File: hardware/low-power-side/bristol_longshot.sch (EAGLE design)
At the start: 80 parts, among them U1 SAM_D20E, U10 ADP1607ACPZN-R7, U11 TPS73118DBVT, U12 TPS73118DBVT, U14 SIT1552, U15 LIS2DH, U16 SIT1552, U2 SI4060, U3 SE880, U4 SST25WF040BT-40I/NP, U5 TG-5006CJ, U6 TG-5006CJ, U7 TPS3123, U8 SN74LVC1G32DCKR, U9 MS5607-02BA03

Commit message: [low-power] v0.986.8. Changed memory pads, GPS LDO and specified SAMD20E18A-MN with more flash and higher grade packaging
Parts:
- removed U4: SST25WF040BT-40I/NP, fbri:SST25WF040BT-40I/NP
- added U$80: SST25WF040BT-40I/NP, fbri:SST25WF040BT-40I/NP
- C11: value 10nF -> DNP
- U12: value TPS73118DBVT -> MIC94310-GYM5
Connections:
- net 1.8V: now also C22.P$1, U$80.!HOLD, U$80.VDD; no longer C14.P$1, U4.!HOLD, U4.VDD
- net GND: now also U$80.VSS; no longer U4.GND_PAD, U4.VSS
- net MEM_CSN: now also U$80.!CE; no longer U4.!CE
- net MEM_MISO: now also U$80.SO/SIO1; no longer U4.SO/SIO1
- net MEM_MOSI: now also U$80.SI/SIO0; no longer U4.SI/SIO0
- net MEM_SCK: now also U$80.SCK; no longer U4.SCK
- net MEM_WPN: now also U$80.!WP; no longer U4.!WP
- net TCXO_VDD1: now also C14.P$1; no longer C22.P$1
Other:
- note added: "XFL4020 is better than VLF302512MT-2R2M used for datasheet efficiency measurements"
- moved on the sheet: C14, C22
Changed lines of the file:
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@@
 <part name="C17" library="microbuilder_v3" deviceset="CAP_CERAMIC" device="_0402" value="100nF"/>
 <part name="U$78" library="microbuilder_v3" deviceset="GND" device=""/>
-<part name="U4" library="fbri" deviceset="SST25WF040BT-40I/NP" device=""/>
 <part name="U$22" library="microbuilder_v3" deviceset="GND" device=""/>
 <part name="JTAG1" library="microbuilder_v3" deviceset="JTAG-CORTEXM3" device="SMT"/>
@@
 <part name="L9" library="Coilcraft_XAL" deviceset="EPL2010" device="" value="EPL2010-2.2µH"/>
 <part name="C27" library="microbuilder_v3" deviceset="CAP_CERAMIC" device="_0402" value="1nF"/>
-<part name="C22" library="microbuilder_v3" deviceset="CAP_CERAMIC" device="_0402" value="100nF"/>
+<part name="C14" library="microbuilder_v3" deviceset="CAP_CERAMIC" device="_0402" value="100nF"/>
 <part name="C31" library="resistor" deviceset="C-EU" device="C0603K" value="10µF"/>
 <part name="U11" library="TPS73118DVBT" deviceset="TPS73118DBVT" device=""/>
@@
 <part name="U14" library="fbri" deviceset="SIT1552" device=""/>
 <part name="U$71" library="microbuilder_v3" deviceset="GND" device=""/>
-<part name="U12" library="TPS73118DVBT" deviceset="TPS73118DBVT" device=""/>
+<part name="U12" library="TPS73118DVBT" deviceset="TPS73118DBVT" device="" value="MIC94310-GYM5"/>
 <part name="U$70" library="microbuilder_v3" deviceset="1.8V" device=""/>
-<part name="C11" library="microbuilder_v3" deviceset="CAP_CERAMIC" device="_0402" value="10nF"/>
+<part name="C11" library="microbuilder_v3" deviceset="CAP_CERAMIC" device="_0402" value="DNP"/>
 <part name="U$84" library="microbuilder_v3" deviceset="GND" device=""/>
 <part name="U$85" library="microbuilder_v3" deviceset="GND" device=""/>
-<part name="C14" library="microbuilder_v3" deviceset="CAP_CERAMIC" device="_0402" value="100nF"/>
+<part name="C22" library="microbuilder_v3" deviceset="CAP_CERAMIC" device="_0402" value="100nF"/>
 <part name="U$65" library="microbuilder_v3" deviceset="GND" device=""/>
 <part name="U16" library="fbri" deviceset="SIT1552" device=""/>
@@
 <part name="U$76" library="microbuilder_v3" deviceset="GND" device=""/>
 <part name="U$77" library="microbuilder_v3" deviceset="1.8V" device=""/>
+<part name="U$80" library="fbri" deviceset="SST25WF040BT-40I/NP" device=""/>
 </parts>
 <sheets>
@@
 <text x="256.54" y="122.428" size="1.27" layer="97" font="vector" ratio="11" distance="100">C15 in close
 proximity</text>
+<text x="27.94" y="66.548" size="1.27" layer="97" font="vector" ratio="11" distance="100">XFL4020 is better than
+VLF302512MT-2R2M used for
+datasheet efficiency
+measurements</text>
 </plain>
 <instances>
@@
 <instance part="C17" gate="G$1" x="20.32" y="172.72"/>
 <instance part="U$78" gate="G$1" x="20.32" y="165.1"/>
-<instance part="U4" gate="G$1" x="226.06" y="83.82"/>
 <instance part="U$22" gate="G$1" x="55.88" y="213.36" rot="MR0"/>
 <instance part="JTAG1" gate="G$1" x="43.18" y="226.06" rot="MR0"/>
@@
 <instance part="L9" gate="G$1" x="706.12" y="106.68"/>
 <instance part="C27" gate="G$1" x="726.44" y="91.44"/>
-<instance part="C22" gate="G$1" x="739.14" y="91.44"/>
+<instance part="C14" gate="G$1" x="739.14" y="91.44"/>
 <instance part="C31" gate="G$1" x="751.84" y="93.98"/>
 <instance part="U11" gate="A" x="492.76" y="208.28"/>
@@
 <instance part="U$84" gate="G$1" x="502.92" y="76.2"/>
 <instance part="U$85" gate="G$1" x="492.76" y="76.2"/>
-<instance part="C14" gate="G$1" x="459.74" y="88.9"/>
+<instance part="C22" gate="G$1" x="459.74" y="88.9"/>
 <instance part="U$65" gate="G$1" x="459.74" y="76.2"/>
 <instance part="U16" gate="G$1" x="241.3" y="121.92" rot="MR0"/>
@@
 <instance part="U$76" gate="G$1" x="134.62" y="213.36" rot="MR0"/>
 <instance part="U$77" gate="G$1" x="134.62" y="254" rot="MR0"/>
+<instance part="U$80" gate="G$1" x="228.6" y="83.82"/>
 </instances>
 <busses>
@@
 <segment>
 <pinref part="U$39" gate="G$1" pin="GND"/>
-<wire x1="205.74" y1="78.74" x2="195.58" y2="78.74" width="0.1524" layer="91"/>
+<wire x1="208.28" y1="78.74" x2="195.58" y2="78.74" width="0.1524" layer="91"/>
 <wire x1="195.58" y1="78.74" x2="185.42" y2="78.74" width="0.1524" layer="91"/>
-<wire x1="185.42" y1="78.74" x2="185.42" y2="76.2" width="0.1524" layer="91"/>
-<wire x1="185.42" y1="76.2" x2="185.42" y2="73.66" width="0.1524" layer="91"/>
-<wire x1="205.74" y1="76.2" x2="185.42" y2="76.2" width="0.1524" layer="91"/>
-<junction x="185.42" y="76.2"/>
+<wire x1="185.42" y1="78.74" x2="185.42" y2="73.66" width="0.1524" layer="91"/>
 <pinref part="C21" gate="G$1" pin="P$2"/>
 <wire x1="185.42" y1="78.74" x2="185.42" y2="81.28" width="0.1524" layer="91"/>
 <junction x="185.42" y="78.74"/>
-<pinref part="U4" gate="G$1" pin="VSS"/>
-<pinref part="U4" gate="G$1" pin="GND_PAD"/>
 <pinref part="C10" gate="G$1" pin="P$2"/>
 <wire x1="195.58" y1="81.28" x2="195.58" y2="78.74" width="0.1524" layer="91"/>
 <junction x="195.58" y="78.74"/>
+<pinref part="U$80" gate="G$1" pin="VSS"/>
 </segment>
 <segment>
@@
 <wire x1="726.44" y1="88.9" x2="739.14" y2="88.9" width="0.1524" layer="91"/>
 <junction x="726.44" y="88.9"/>
-<pinref part="C22" gate="G$1" pin="P$2"/>
+<pinref part="C14" gate="G$1" pin="P$2"/>
 <wire x1="739.14" y1="88.9" x2="751.84" y2="88.9" width="0.1524" layer="91"/>
 <junction x="739.14" y="88.9"/>
@@
 </segment>
 <segment>
-<pinref part="C14" gate="G$1" pin="P$2"/>
+<pinref part="C22" gate="G$1" pin="P$2"/>
 <pinref part="U$65" gate="G$1" pin="GND"/>
 <wire x1="459.74" y1="86.36" x2="459.74" y2="78.74" width="0.1524" layer="91"/>
@@
 <net name="MEM_MOSI" class="0">
 <segment>
-<wire x1="246.38" y1="91.44" x2="264.16" y2="91.44" width="0.1524" layer="91"/>
+<wire x1="248.92" y1="91.44" x2="264.16" y2="91.44" width="0.1524" layer="91"/>
 <label x="251.46" y="91.44" size="1.778" layer="95" ratio="11"/>
-<pinref part="U4" gate="G$1" pin="SI/SIO0"/>
+<pinref part="U$80" gate="G$1" pin="SI/SIO0"/>
 </segment>
 <segment>
@@
 <net name="MEM_CSN" class="0">
 <segment>
-<wire x1="264.16" y1="78.74" x2="246.38" y2="78.74" width="0.1524" layer="91"/>
+<wire x1="264.16" y1="78.74" x2="248.92" y2="78.74" width="0.1524" layer="91"/>
 <label x="251.46" y="78.74" size="1.778" layer="95" ratio="11"/>
-<pinref part="U4" gate="G$1" pin="!CE"/>
+<pinref part="U$80" gate="G$1" pin="!CE"/>
 </segment>
 <segment>
@@
 <net name="MEM_WPN" class="0">
 <segment>
-<wire x1="246.38" y1="81.28" x2="264.16" y2="81.28" width="0.1524" layer="91"/>
+<wire x1="248.92" y1="81.28" x2="264.16" y2="81.28" width="0.1524" layer="91"/>
 <label x="251.46" y="81.28" size="1.778" layer="95" ratio="11"/>
-<pinref part="U4" gate="G$1" pin="!WP"/>
+<pinref part="U$80" gate="G$1" pin="!WP"/>
 </segment>
 </net>
@@
 <net name="MEM_SCK" class="0">
 <segment>
-<wire x1="246.38" y1="86.36" x2="264.16" y2="86.36" width="0.1524" layer="91"/>
+<wire x1="248.92" y1="86.36" x2="264.16" y2="86.36" width="0.1524" layer="91"/>
 <label x="251.46" y="86.36" size="1.778" layer="95" ratio="11"/>
-<pinref part="U4" gate="G$1" pin="SCK"/>
+<pinref part="U$80" gate="G$1" pin="SCK"/>
 </segment>
 <segment>
@@
 <net name="MEM_MISO" class="0">
 <segment>
-<wire x1="246.38" y1="88.9" x2="264.16" y2="88.9" width="0.1524" layer="91"/>
+<wire x1="248.92" y1="88.9" x2="264.16" y2="88.9" width="0.1524" layer="91"/>
 <label x="251.46" y="88.9" size="1.778" layer="95" ratio="11"/>
-<pinref part="U4" gate="G$1" pin="SO/SIO1"/>
+<pinref part="U$80" gate="G$1" pin="SO/SIO1"/>
 </segment>
 <segment>
@@
 <wire x1="726.44" y1="99.06" x2="739.14" y2="99.06" width="0.1524" layer="91"/>
 <wire x1="739.14" y1="99.06" x2="751.84" y2="99.06" width="0.1524" layer="91"/>
-<pinref part="C22" gate="G$1" pin="P$1"/>
+<pinref part="C14" gate="G$1" pin="P$1"/>
 <wire x1="739.14" y1="96.52" x2="739.14" y2="99.06" width="0.1524" layer="91"/>
 <pinref part="C27" gate="G$1" pin="P$1"/>
@@
 <segment>
 <pinref part="U$40" gate="G$1" pin="1.8V"/>
-<wire x1="205.74" y1="91.44" x2="203.2" y2="91.44" width="0.1524" layer="91"/>
+<wire x1="208.28" y1="91.44" x2="203.2" y2="91.44" width="0.1524" layer="91"/>
 <wire x1="203.2" y1="91.44" x2="195.58" y2="91.44" width="0.1524" layer="91"/>
 <wire x1="195.58" y1="91.44" x2="185.42" y2="91.44" width="0.1524" layer="91"/>
@@
 <wire x1="185.42" y1="88.9" x2="185.42" y2="91.44" width="0.1524" layer="91"/>
 <junction x="185.42" y="91.44"/>
-<pinref part="U4" gate="G$1" pin="VDD"/>
-<pinref part="U4" gate="G$1" pin="!HOLD"/>
-<wire x1="205.74" y1="86.36" x2="203.2" y2="86.36" width="0.1524" layer="91"/>
+<wire x1="208.28" y1="86.36" x2="203.2" y2="86.36" width="0.1524" layer="91"/>
 <wire x1="203.2" y1="86.36" x2="203.2" y2="91.44" width="0.1524" layer="91"/>
 <junction x="203.2" y="91.44"/>
@@
 <wire x1="195.58" y1="91.44" x2="195.58" y2="88.9" width="0.1524" layer="91"/>
 <junction x="195.58" y="91.44"/>
+<pinref part="U$80" gate="G$1" pin="VDD"/>
+<pinref part="U$80" gate="G$1" pin="!HOLD"/>
 </segment>
 <segment>
@@
 <wire x1="505.46" y1="101.6" x2="459.74" y2="101.6" width="0.1524" layer="91"/>
 <wire x1="459.74" y1="101.6" x2="459.74" y2="106.68" width="0.1524" layer="91"/>
-<pinref part="C14" gate="G$1" pin="P$1"/>
+<pinref part="C22" gate="G$1" pin="P$1"/>
 <wire x1="459.74" y1="101.6" x2="459.74" y2="93.98" width="0.1524" layer="91"/>
 <junction x="459.74" y="101.6"/>

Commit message: [low-power] |v0.987.0|Low Power. Added 32kHz TCXO RC filters, replaced GPS LDO with MOSFET, remove IMU, vreg on b/out, update SE880 footprint, Watchdog, Radio, filter design
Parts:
- removed CBO1, CBO2: 1µF, microbuilder_v3:CAP_CERAMIC_0402
- removed CBO3: 10nF, microbuilder_v3:CAP_CERAMIC_0402
- removed U$80: SST25WF040BT-40I/NP, fbri:SST25WF040BT-40I/NP
- removed U15: LIS2DH, fbri:LIS2DH
- removed UBO1: TPS73118DBVT, TPS73118DVBT:TPS73118DBVT
- added C4: 15pF, microbuilder_v3:CAP_CERAMIC_0402
- added C7: 100nF, microbuilder_v3:CAP_CERAMIC_0402
- added FB3: (no value), microbuilder_v3:FERRITE_0402
- added JP2: (no value), SparkFun:M02LOCK
- added Q1: NX2301P, nxp:NX2301P
- added R14: 100kΩ, microbuilder_v3:RESISTOR_0402
- added R15, R16: 1MΩ, microbuilder_v3:RESISTOR_0402
- added U4: SST25WF040BT-40I/NP, fbri:SST25WF040BT-40I/NP
- C0': value 15pF -> DNP
- C11: value DNP -> 15pF
- C28: value 1µF -> 2.2µF
- L0': value 56nH -> DNP
- LC: value 220nH -> 470nH
- R10, R11, R13: value 10kΩ -> 100kΩ
- R12: value 0Ω -> 100kΩ
- R5, R6, R7: value 100kΩ -> 10kΩ
- R8: value 43kΩ -> 10kΩ
- R9: value 100kΩ -> 43kΩ
- U12: value MIC94310-GYM5 -> 74LVC1G04GW; device TPS73118DVBT:TPS73118DBVT -> 74LVC1G04GW_inverter:74LVC1G04GW
- U2: value SI4060 -> SI4461
- U7: value TPS3123 -> ADM6823WYRJZ
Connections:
- net TCXO_VDD1 renamed SE_TCXO_VDD
- removed net GPS_REG_NR: C11.P$1, U12.NR/FB
- removed net JTAG_VIN: CBO1.P$1, JTAG1.1, R12.1, UBO1.EN, UBO1.IN
- removed net JTAG_VREG_NR: CBO3.P$1, UBO1.NR/FB
- new net GPS_VDD_SWITCHED: C28.P$1, C7.P$1, C9.P$1, Q1.D, U14.VCC, U3.VDD, U3.VKA
- new net LF_CLOCK_OUT: R7.2, U16.OUT
- new net RESET: Q1.G, R15.1, U12.Y
- new net SE800_LF_OUT: R8.2, U14.OUT
- net !RESET: now also U12.A; no longer U12.EN
- net 1.2V: now also JP1.1, R14.2; no longer R13.2
- net 1.8V: now also FB3.P$2, JTAG1.1, R5.2, R6.2, R9.2, U4.!HOLD, U4.VDD; no longer C22.P$1, CBO2.P$1, R10.2, R11.2, R12.2, R8.2, U$80.!HOLD, U$80.VDD, U12.IN, U15.CS, U15.SDO/SA0, U15.VDD, U15.VDD_IO, UBO1.OUT
- net BOOST_EN: now also JP2.1, R14.1; no longer JP1.2, R13.1
- net EXT_THERMISTOR_SENSE: now also R11.2; no longer R7.2
- net FB: now also R10.2, R9.1; no longer R8.1, R9.2
- net GND: now also C4.P$2, C7.P$2, JP1.2, JP2.2, R10.1, R11.1, R13.1, R16.1, U4.VSS; no longer CBO1.P$2, CBO2.P$2, CBO3.P$2, JP1.1, R5.1, R7.1, R9.1, U$80.VSS, U15.GND, U15.GND1, U15.GND2, UBO1.GND
- net GPS_VDD: now also C22.P$1, FB3.P$1, Q1.S, R15.2, U12.VCC; no longer C28.P$1, C9.P$1, U12.OUT, U14.VCC, U3.VDD, U3.VKA
- net LF_CLOCK: now also C11.P$1, R7.1; no longer U16.OUT
- net MEM_CSN: now also U4.!CE; no longer U$80.!CE
- net MEM_MISO: now also U4.SO/SIO1; no longer U$80.SO/SIO1
- net MEM_MOSI: now also U4.SI/SIO0; no longer U$80.SI/SIO0
- net MEM_SCK: now also U4.SCK; no longer U$80.SCK
- net MEM_WPN: now also U4.!WP; no longer U$80.!WP
- net RTC_XI: now also C4.P$1, R8.1; no longer U14.OUT
- net SAM_XOSC: now also R12.1, R13.2; no longer R5.2, R6.1
- net SCL: now also R6.1; no longer R11.1, U15.SCL/SPC
- net SDA: now also R5.1; no longer R10.1, U15.SDA/SDI/SDO
- net TCXO_VDD: now also R12.2; no longer R6.2
- net WDI!RESET: now also R16.2
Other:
- note added: "1.2V supply for power measurements"
- note added: "140ms min high on reset"
- note added: "140ms min low on reset"
- note added: "Connect to disable boost reg"
- note added: "Input C < 15pF"
- note added: "Nominal output voltage 1.80V When using 0.1% resistors most of the variablity is in V_FB Specified 1.76V - 1.85V"
- note added: "R_DSon = 0.2Ω @ V_GS = -1.8V, Id = 0.1A"
- note added: "Regulator included to cycle power on system reset"
- note added: "Use ADM6823WYRJZ"
- note added: "V_GSth = -1.1V @ Id = 0.1A"
- note added: "Vth = 1.62-1.71V t_RP = 140-280ms t_WD = 1.12-2.4s"
- note added: "approx. 20mV dropout"
- note added: "f_0 = 500kHz-1MHz"
- note added: "t_WD is 0.93x nominal at -40ºC"
- note removed: "180ms low on reset"
- note removed: "LIS2D 3-axis accelerometer"
- note removed: "Nominal output voltage 1.80V Using 0.1% resistors most of the variablity is in V_FB Specified 1.76V - 1.85V"
- note removed: "Regulator included to cycle power on failure, also for power conditioning"
- moved on the sheet: C10, C11, C14, C19, C21, C22, C26, C27, C28, C31, C9, JP1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

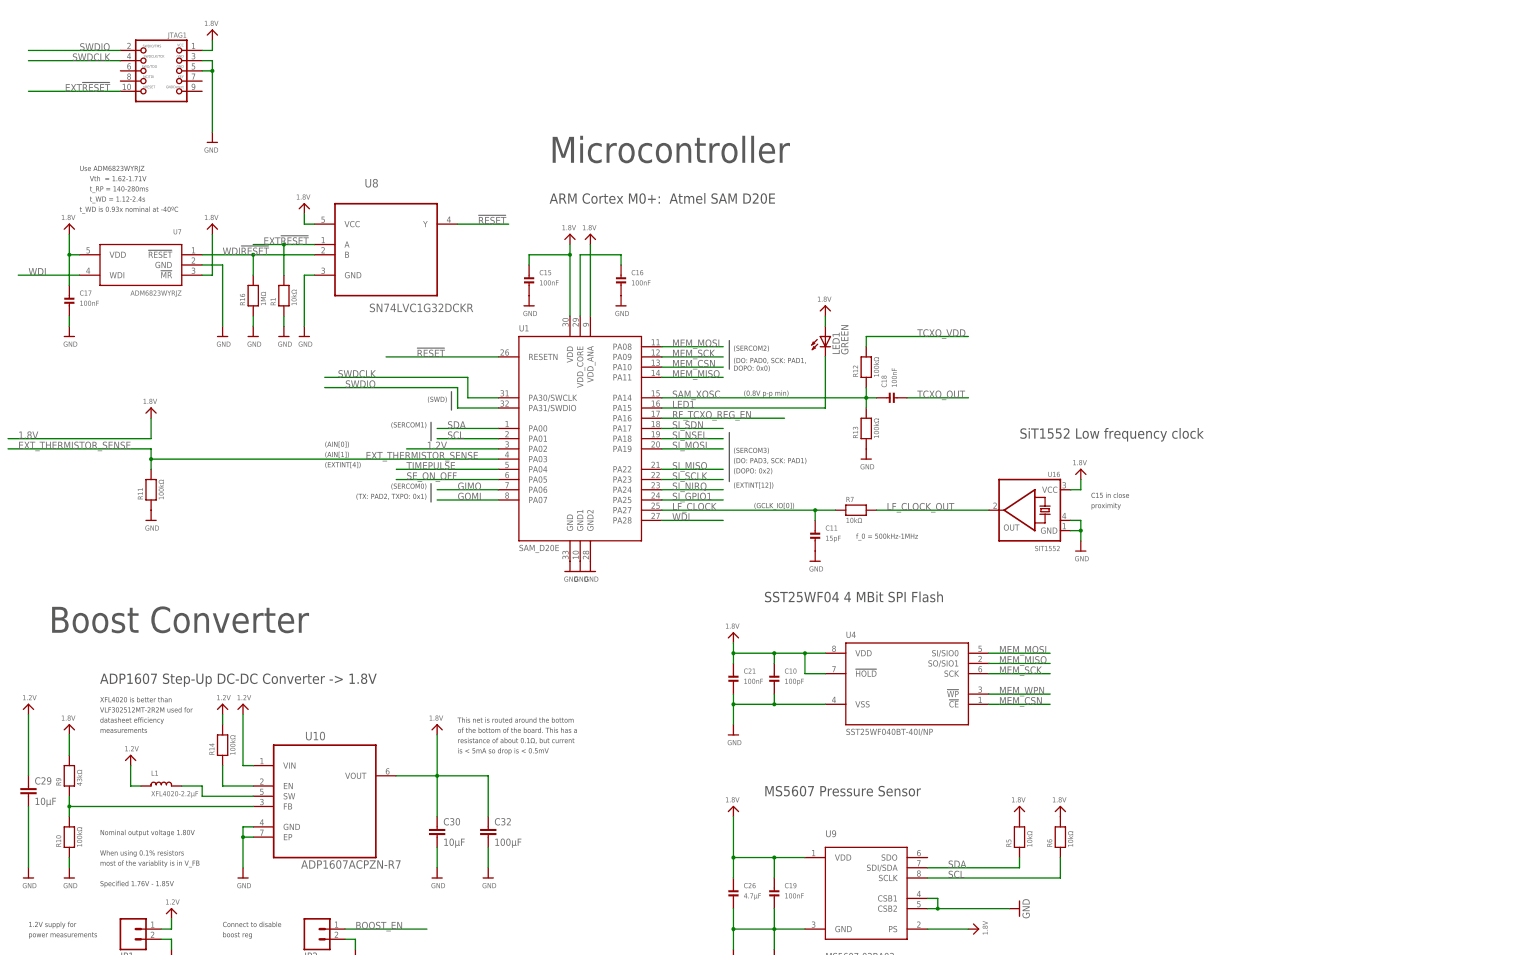
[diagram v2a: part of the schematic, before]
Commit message: [low-power] |v0.987.1|Low Power. Switch LF Clock to XOSC32K pin from GCLK_IO[0]. Allows feed to any GCLK. Bit-bang i2c instead
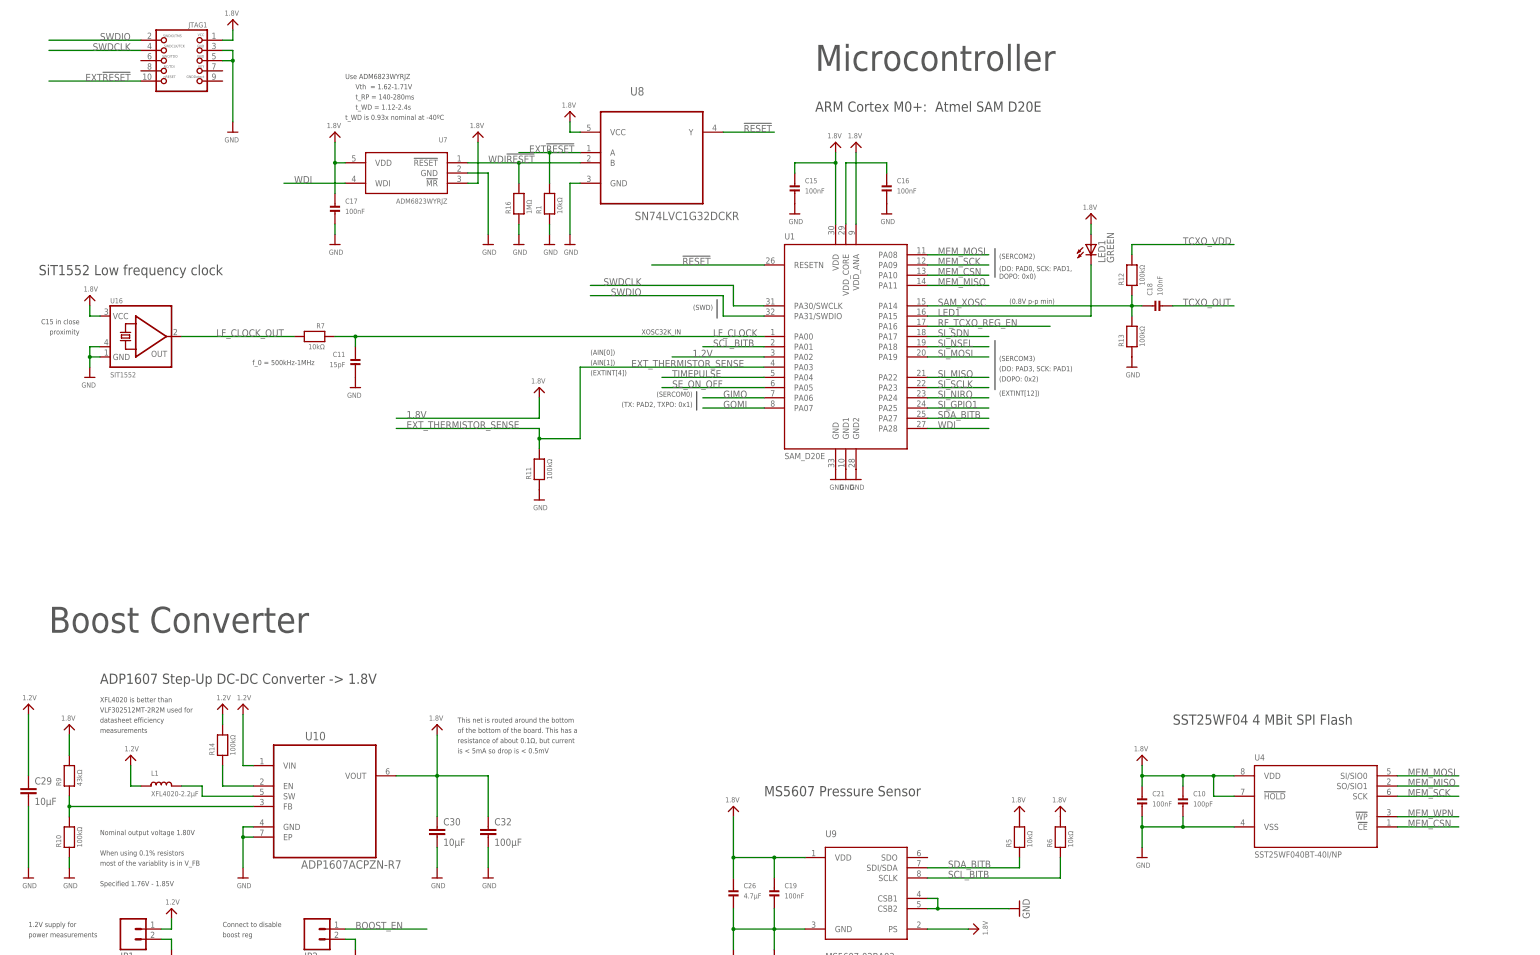
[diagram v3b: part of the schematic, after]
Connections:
- net SCL renamed SCL_BITB
- removed net SDA: R5.1, U1.PA00, U9.SDI/SDA
- new net SDA_BITB: R5.1, U1.PA27, U9.SDI/SDA
- net LF_CLOCK: now also U1.PA00; no longer U1.PA27
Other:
- note added: "XOSC32K_IN"
- note removed: "(GCLK_IO[0])"
- note removed: "(SERCOM1)"
- moved on the sheet: C10, C11, C15, C16, C17, C18, C21, JTAG1, LED1, R1, R11, R12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
